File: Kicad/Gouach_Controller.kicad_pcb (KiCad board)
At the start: 4 copper layers, 41 x 104 mm, 135 parts, among them J1 HALL/Encoder, J10 USB, J11 CANBUS, J12 Serial, J2 SWD, J3 Peripherals, J4 IN+, J5 IN-, J6 MOTOR3, J7 MOTOR2, J8 MOTOR1, Q1 IRFB7530, Q2 IRFB7530, Q3 IRFB7530, Q4 IRFB7530, Q5 IRFB7530, Q6 IRFB7530, U1 STM32F405RGT6, U2 TC2117, U3 DRV8302, U4 SN65HVD232, U5 TPS54360DDA, Y2 8MHz

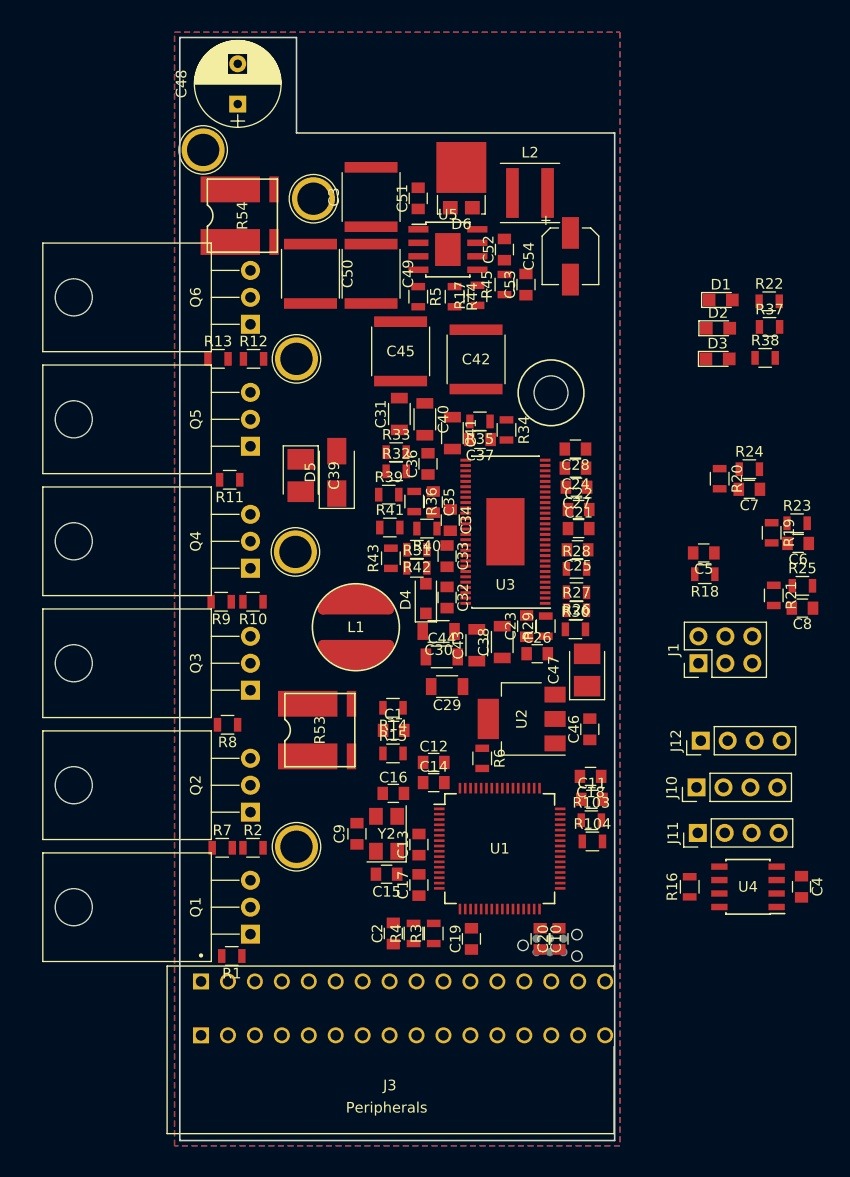
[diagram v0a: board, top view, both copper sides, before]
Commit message: Passives changed from 0805 to 0603
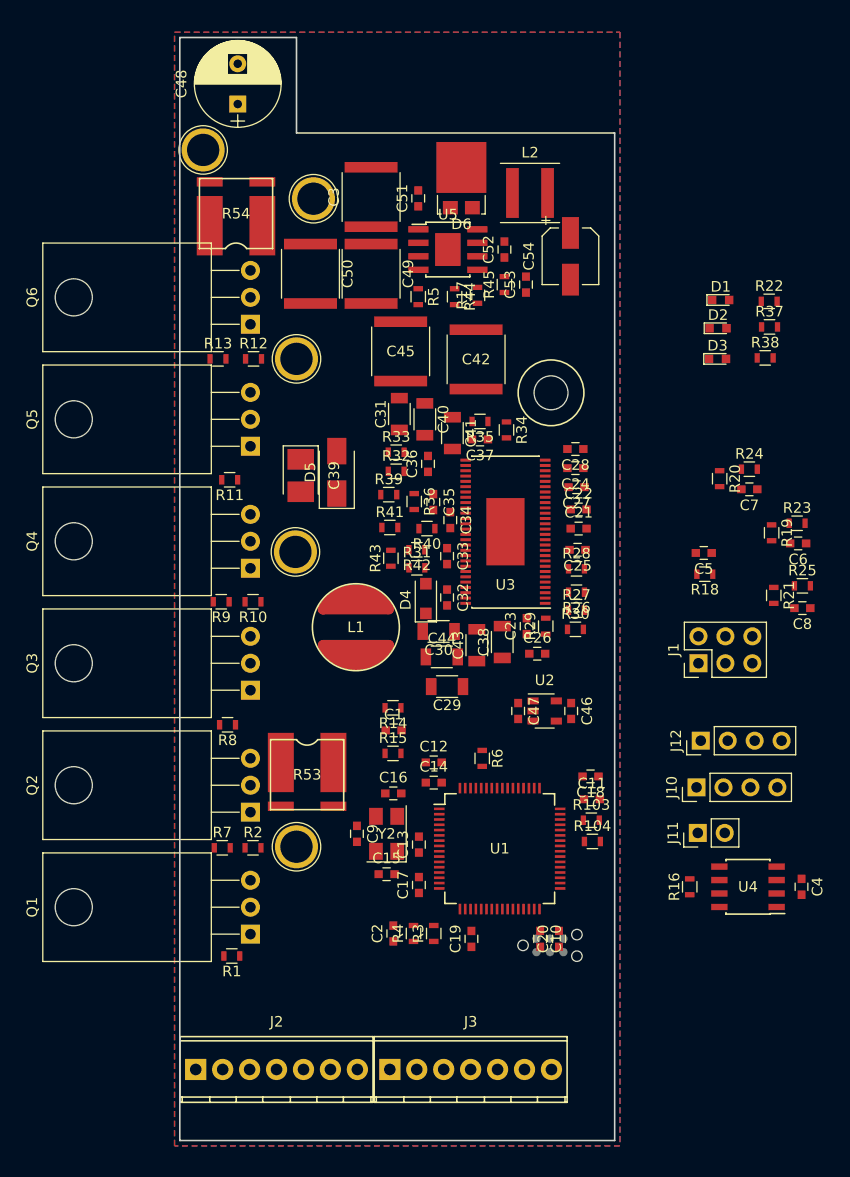
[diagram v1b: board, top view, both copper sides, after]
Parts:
- added J2: Peripherals, Romain:TerminalBlock_Phoenix_MPT-2.54mm_7pol, F.Cu at (101.5, 143.3)
- C1, C10, C11, C12, C13, C14, C15, C16, C17, C18, C19, C2, C20, C21, C22, C23, C24, C25, C26, C27, C28, C32, C33, C34, C35, C36, C37, C4, C5, C51, C52, C53, C6, C7, C8, C9: footprint Capacitors_SMD:C_0805 -> Capacitors_SMD:C_0603
- C46: value 2.2uF -> 10uF; footprint Capacitors_SMD:C_0805 -> Capacitors_SMD:C_0603
- C47: value 15uF/100V -> 10uF; footprint Capacitors_Tantalum_SMD:CP_Tantalum_Case-B_EIA-3528-21_Reflow -> Capacitors_SMD:C_0603
- D1, D2, D3: footprint LEDs:LED_0805 -> LEDs:LED_0603
- J11: footprint Pin_Headers:Pin_Header_Straight_1x04_Pitch2.54mm -> Pin_Headers:Pin_Header_Straight_1x02_Pitch2.54mm
- J3: footprint Romain:TBL009-254-16BE-2BE -> Romain:TerminalBlock_Phoenix_MPT-2.54mm_7pol
- Q1, Q2, Q3, Q4, Q5, Q6: footprint TO_SOT_Packages_THT:TO-220-3_Horizontal -> Romain:TO-220-3_Horizontal
- R1, R10, R103, R104, R11, R12, R13, R14, R15, R16, R17, R18, R19, R2, R20, R21, R22, R23, R24, R25, R26, R27, R28, R29, R3, R30, R31, R32, R33, R34, R35, R36, R37, R38, R39, R4, R40, R41, R42, R43, R44, R45, R5, R6, R7, R8, R9: footprint Resistors_SMD:R_0805 -> Resistors_SMD:R_0603
- U2: value TC2117 -> XC6220B331MR; footprint TO_SOT_Packages_SMD:SOT-223-3_TabPin2 -> TO_SOT_Packages_SMD:SOT-23-5
- moved J3 19.6 mm to (119.8, 143.3)
- moved C47 7.56 mm to (131.9, 109.5), turned to 270 degrees
- moved R53 4.37 mm to (112.0, 115.5), turned to 180 degrees
- moved C46 2.46 mm to (136.9, 109.5), turned to 270 degrees
- moved U2 2.29 mm to (134.4, 109.5), turned to 0 degrees
- moved R54 0.63 mm to (105.3, 62.6), turned to 0 degrees
- renumbered J2 to J9
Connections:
- C47 pad 1: +3V3 -> +5V
- J11 pad 1: +5V -> /CAN Transceiver/CAN_P
- J11 pad 2: /CAN Transceiver/CAN_P -> /CAN Transceiver/CAN_N
- J3 pad 1: +5V -> GND
- J3 pad 2: /ADC_THROTTLE -> +5V
- J3 pad 3: GND -> /IO_BRAKE
- J3 pad 4: +5V -> /ADC_BRAKE
- J3 pad 5: /PFS -> GND
- J3 pad 6: /ADC_TORQUE -> Net-(J3-Pad6)
- J3 pad 7: /CRUISE -> GND
- U1 pad 20: /MCU/TX_SDA_NSS -> /TX
- U1 pad 23: /MCU/RX_SCL_MOSI -> /RX
- U1 pad 29: /MCU/RX_SCL_MOSI -> /RX
- U1 pad 30: /MCU/TX_SDA_NSS -> /TX
- U1 pad 37: /MCU/TX_SDA_NSS -> /TX
- U1 pad 38: /MCU/RX_SCL_MOSI -> /RX
- U2 pad 1: GND -> +5V
- U2 pad 2: +3V3 -> GND

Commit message: Components placed
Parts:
- removed R103, R104: 22R, Resistors_SMD:R_0603
- added Q7: DMN3300U, TO_SOT_Packages_SMD:SOT-23, F.Cu at (132.8, 66.8)
- added R46: 100R, Resistors_SMD:R_0603, F.Cu at (129.7, 67.8)
- added R47: 10k, Resistors_SMD:R_0603, F.Cu at (129.7, 65.9)
- added U6: USBLC6-2SC6, TO_SOT_Packages_SMD:SOT-23-6, F.Cu at (135.4, 70.7)
- C12, C14, C16, C17, C18, C19, C20: value 2.2uF -> 100nF
- C3, C49, C50: footprint Capacitors_SMD:C_2220 -> Capacitors_SMD:C_1210
- D4: value 60V 2A -> 60V
- D6: value 100V -> 60V; footprint TO_SOT_Packages_SMD:TO-277A -> Diodes_SMD:D_SOD-123F
- J9: moved to F.Cu
- moved D1 78.9 mm to (138.9, 148.7), turned to 180 degrees
- moved R37 75.9 mm to (138.9, 147.3), turned to 180 degrees
- moved D2 73.4 mm to (138.9, 145.9), turned to 180 degrees
- moved R22 72.7 mm to (138.9, 141.7), turned to 180 degrees
- moved R38 70.2 mm to (138.9, 144.5), turned to 180 degrees
- moved D3 67.8 mm to (138.9, 143.1), turned to 180 degrees
- moved R24 54.6 mm to (118.5, 128.4), turned to 90 degrees
- moved R20 54.3 mm to (117.8, 130.6), turned to 180 degrees
- moved C7 54.1 mm to (117.0, 128.4), turned to 270 degrees
- moved R18 53.5 mm to (116.8, 139.0)
- moved J12 53.4 mm to (101.8, 136.9)
- moved C5 53.3 mm to (119.8, 139.0), turned to 0 degrees
- moved C8 53.1 mm to (114.0, 128.4), turned to 270 degrees
- moved R25 53.0 mm to (115.5, 128.4), turned to 90 degrees
- moved R21 52.2 mm to (114.7, 130.6), turned to 180 degrees
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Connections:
- D4 pad 1: GND -> Net-(C32-Pad1)
- D4 pad 2: Net-(C32-Pad1) -> GND
- D5 pad 1: GND -> +5V
- D5 pad 2: +5V -> GND
- J10 pad 2: /D+ -> /D-
- J10 pad 3: /D- -> /D+
- Q3 pad 3: /MOSFETs driver/H2_VS -> /MOSFETs driver/H3_VS
- Q4 pad 2: /MOSFETs driver/H2_VS -> /MOSFETs driver/H3_VS
- Q4 pad 3: GND -> /MOSFETs driver/H3_LOW
- Q5 pad 3: /MOSFETs driver/H3_VS -> /MOSFETs driver/H2_VS
- Q6 pad 2: /MOSFETs driver/H3_VS -> /MOSFETs driver/H2_VS
- Q6 pad 3: /MOSFETs driver/H3_LOW -> GND
- R10 pad 2: Net-(Q4-Pad1) -> Net-(Q6-Pad1)
- R11 pad 1: Net-(Q5-Pad1) -> Net-(Q3-Pad1)
- R12 pad 1: Net-(Q6-Pad1) -> Net-(Q4-Pad1)
- R13 pad 2: Net-(Q6-Pad1) -> Net-(Q4-Pad1)
- R8 pad 1: Net-(Q3-Pad1) -> Net-(Q5-Pad1)
- R9 pad 1: Net-(Q4-Pad1) -> Net-(Q6-Pad1)
- U1 pad 11: Net-(U1-Pad11) -> /MCU/LAMP_CMD
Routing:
- net +5V: track 0.00 -> 48.6 mm
- net +3V3: track 0.00 -> 21.4 mm, vias 0 -> 3
- net +BATT: track 0.00 -> 15.5 mm, vias 0 -> 119
- net +5VP: track 0.00 -> 12.2 mm
- net Net-(C24-Pad2): track 0.00 -> 11.5 mm, vias 0 -> 2
- net GND: track 0.00 -> 9.10 mm
- net /MCU/OSC_IN: track 0.00 -> 8.96 mm
- net Net-(C51-Pad2): track 0.00 -> 8.15 mm, vias 0 -> 2
- net /MCU/OSC_OUT: track 0.00 -> 5.89 mm
- net /CAN Transceiver/CAN_P: track 0.00 -> 5.40 mm
- net /CAN Transceiver/CAN_N: track 0.00 -> 5.40 mm
- net Net-(C21-Pad1): track 0.00 -> 5.37 mm
- net /Filters/HALL1_IN: track 0.00 -> 5.06 mm
- net /Filters/HALL3_IN: track 0.00 -> 5.05 mm
- net /Filters/HALL2_IN: track 0.00 -> 4.85 mm
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- added copper zone on F.Cu, net +5VP
- added copper zone on B.Cu, net +BATT
- added copper zone on F.Cu, net +BATT
- added copper zone on GND, net +BATT
- added copper zone on GND2, net +BATT
- added copper zone on F.Cu, net Net-(C51-Pad2)
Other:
- outline, holes or cut-outs redrawn
- net class Default: clearance 0.1778 -> 0.2; trace_width 0.2032 -> 0.254; via_dia 0.8 -> 0.5; via_drill 0.5 -> 0.3
- rule trace_clearance: 0.1778 -> 0.2
- rule via_min_drill: 0.5 -> 0.3
- rule via_min_size: 0.8 -> 0.5
- board text added: "5V Thr GND 5V PFS Trq Crs GND 5V BkD BkA GND Lmp GND"

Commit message: Routing done
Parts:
- removed C42, C45: 15uF/100V, Capacitors_SMD:C_2220
- added C55: 2.2uF, Capacitors_SMD:C_1210, F.Cu at (122.2, 114.6)
- added C56: 100nF, Capacitors_SMD:C_0603, F.Cu at (121.5, 127.4)
- added G***: LOGO, Romain:logo, B.Cu at (120.4, 137.3)
- C22, C24: value 2.2uF -> NP
- C25, C28: value 2.2uF -> 1uF
- C29: value 10uF/60V -> 2.2uF; footprint Capacitors_SMD:C_1206 -> Capacitors_SMD:C_1210
- C30, C38: value 10uF/60V -> 100nF; footprint Capacitors_SMD:C_1206 -> Capacitors_SMD:C_0805
- C31: value 10uF/60V -> 47uF; footprint Capacitors_SMD:C_1206 -> Capacitors_SMD:C_1210
- C33, C34, C35: value 220nF -> 100nF
- C36, C37: value 2.2nF -> 1nF
- C39: value 15uF/100V -> 1uF; footprint Capacitors_Tantalum_SMD:CP_Tantalum_Case-B_EIA-3528-21_Reflow -> Capacitors_SMD:C_0603
- C40, C41, C43, C44: value 10uF/60V -> 10uF
- C48: footprint Capacitors_THT:CP_Radial_D8.0mm_P3.80mm -> Romain:Capacitor_Horizontal
- J11: value CANBUS -> CAN
- J12: moved to B.Cu
- J4, J5: footprint Connectors:1pin -> Mounting_Holes:MountingHole_2.7mm_Pad_Via
- J6, J7, J8: footprint Connectors:1pin -> Mounting_Holes:MountingHole_2.2mm_M2_Pad_Via
- moved C3 78.4 mm to (101.9, 136.7), turned to 270 degrees
- moved C50 77.6 mm to (105.2, 136.7), turned to 270 degrees
- moved C49 77.3 mm to (108.5, 136.7), turned to 270 degrees
- moved C54 75.4 mm to (132.4, 135.5)
- moved R45 75.3 mm to (119.9, 138.6)
- moved R44 75.2 mm to (123.1, 138.6), turned to 0 degrees
- moved L2 75.2 mm to (126.4, 134.5)
- moved J12 74.8 mm to (139.4, 72.3), turned to 0 degrees
- moved C52 74.8 mm to (119.2, 135.9)
- moved C53 74.8 mm to (120.7, 135.9)
- moved R5 74.8 mm to (112.4, 139.3)
- moved U5 74.8 mm to (114.5, 135.9)
- moved D6 74.4 mm to (116.4, 131.8)
- moved J11 73.8 mm to (136.6, 61.7), turned to 90 degrees
- moved C51 73.6 mm to (112.4, 132.2), turned to 0 degrees
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- renumbered Q6 to Q4, Q4 to Q6
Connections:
- net +5VP renamed VBUS
- C31 pad 1: +BATT -> +5V
- C40 pad 1: GND -> +BATT
- C40 pad 2: +BATT -> GND
- C41 pad 1: GND -> +BATT
- C41 pad 2: +BATT -> GND
- C43 pad 1: GND -> +BATT
- C43 pad 2: +BATT -> GND
- C44 pad 1: GND -> +BATT
- C44 pad 2: +BATT -> GND
- J1 pad 3: /Filters/TEMP_IN -> GND
- J1 pad 5: GND -> /Filters/TEMP_IN
- Q3 pad 3: /MOSFETs driver/H3_VS -> /MOSFETs driver/H2_VS
- Q5 pad 3: /MOSFETs driver/H2_VS -> /MOSFETs driver/H3_VS
- R11 pad 1: Net-(Q3-Pad1) -> Net-(Q5-Pad1)
- R32 pad 1: /MOSFETs driver/SH1_A -> /MOSFETs driver/SH1+
- R33 pad 1: /MOSFETs driver/SH1_B -> /MOSFETs driver/SH1-
- R34 pad 1: /MOSFETs driver/SH2_A -> /MOSFETs driver/SH2+
- R35 pad 1: /MOSFETs driver/SH2_B -> /MOSFETs driver/SH2-
- R53 pad 1: GND -> /MOSFETs driver/H1_LOW
- R53 pad 2: /MOSFETs driver/SH2_B -> /MOSFETs driver/SH2+
- R53 pad 3: /MOSFETs driver/SH2_A -> /MOSFETs driver/SH2-
- R53 pad 4: /MOSFETs driver/H1_LOW -> GND
- R54 pad 1: GND -> /MOSFETs driver/H3_LOW
- R54 pad 2: /MOSFETs driver/SH1_B -> /MOSFETs driver/SH1+
- R54 pad 3: /MOSFETs driver/SH1_A -> /MOSFETs driver/SH1-
- R54 pad 4: /MOSFETs driver/H3_LOW -> GND
- R8 pad 1: Net-(Q5-Pad1) -> Net-(Q3-Pad1)
- U1 pad 20: /TX -> Net-(U1-Pad20)
- U1 pad 23: /RX -> Net-(U1-Pad23)
- U1 pad 37: /TX -> Net-(U1-Pad37)
- U1 pad 38: /RX -> Net-(U1-Pad38)
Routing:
- net +3V3: track 21.4 -> 207.2 mm, vias 3 -> 10
- net /CRUISE: track 0.00 -> 107.6 mm, vias 0 -> 2
- net /MCU/LED_RED: track 0.00 -> 99.7 mm, vias 0 -> 2
- net /ADC_THROTTLE: track 0.00 -> 99.6 mm, vias 0 -> 2
- net /IO_BRAKE: track 0.00 -> 99.3 mm, vias 0 -> 1
- net /MCU/AN_IN: track 0.00 -> 96.0 mm, vias 0 -> 4
- net /PFS: track 0.00 -> 95.5 mm, vias 0 -> 1
- net /MCU/LED_GREEN: track 0.00 -> 95.5 mm, vias 0 -> 2
- net /ADC_TORQUE: track 0.00 -> 90.9 mm, vias 0 -> 1
- net +5V: track 48.6 -> 138.0 mm, vias 0 -> 4
- net /ADC_BRAKE: track 0.00 -> 87.1 mm, vias 0 -> 1
- net /MCU/LAMP_CMD: track 0.00 -> 84.1 mm, vias 0 -> 2
- net /MCU/USB_D+: track 0.00 -> 77.6 mm, vias 0 -> 2
- net /MCU/USB_D-: track 0.00 -> 76.8 mm, vias 0 -> 2
- net +BATT: track 15.5 -> 84.4 mm, vias 119 -> 131
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- added copper zone on F.Cu, net +5V
- added copper zone on In1.Cu, net +BATT
- added copper zone on In2.Cu, net +BATT
- added copper zone on B.Cu, net /MOSFETs driver/H1_LOW
- added copper zone on F.Cu, net /MOSFETs driver/H1_LOW
- added copper zone on In1.Cu, net /MOSFETs driver/H1_LOW
- added copper zone on In2.Cu, net /MOSFETs driver/H1_LOW
- added copper zone on B.Cu, net /MOSFETs driver/H1_VS
- added copper zone on F.Cu, net /MOSFETs driver/H1_VS
- added copper zone on In1.Cu, net /MOSFETs driver/H1_VS
- added copper zone on In2.Cu, net /MOSFETs driver/H1_VS
- added copper zone on B.Cu, net /MOSFETs driver/H2_VS
- added copper zone on F.Cu, net /MOSFETs driver/H2_VS
- added copper zone on In1.Cu, net /MOSFETs driver/H2_VS
- added copper zone on In2.Cu, net /MOSFETs driver/H2_VS
- added copper zone on B.Cu, net /MOSFETs driver/H3_LOW
- added copper zone on F.Cu, net /MOSFETs driver/H3_LOW
- added copper zone on In1.Cu, net /MOSFETs driver/H3_LOW
- added copper zone on In2.Cu, net /MOSFETs driver/H3_LOW
- added copper zone on B.Cu, net /MOSFETs driver/H3_VS
- added copper zone on F.Cu, net /MOSFETs driver/H3_VS
- added copper zone on In1.Cu, net /MOSFETs driver/H3_VS
- added copper zone on In2.Cu, net /MOSFETs driver/H3_VS
- added copper zone on In1.Cu, net GND
- added copper zone on In2.Cu, net GND
- removed copper zone on GND, net +BATT
- removed copper zone on GND2, net +BATT
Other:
- outline, holes or cut-outs redrawn
- board text added: "+ -"
- board text added: "3/T 2/G 1/5"
- board text added: "5V D- D+ GND"
- board text added: "5V Thr GND 5V PFS Trq Crs"
- board text added: "GND 5V BkD BkA GND Lmp GND"
- board text added: "GND RX TX 5V"
- board text added: "TEMP HALL3 GND HALL2 +5V HALL1"
- board text removed: "5V Thr GND 5V PFS Trq Crs GND 5V BkD BkA GND Lmp GND"

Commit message: Fixed libraries issues
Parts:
- C1, C10, C11, C12, C13, C14, C15, C16, C17, C18, C19, C2, C20, C21, C22, C23, C24, C25, C26, C27, C28, C32, C33, C34, C35, C36, C37, C39, C4, C46, C47, C5, C51, C52, C53, C56, C6, C7, C8, C9: footprint Capacitors_SMD:C_0603 -> Capacitor_SMD:C_0603_1608Metric
- C29, C31, C55: footprint Capacitors_SMD:C_1210 -> Capacitor_SMD:C_1210_3225Metric
- C3, C49, C50: footprint Capacitors_SMD:C_1210 -> Capacitor_SMD:C_1206_3216Metric
- C30, C38: footprint Capacitors_SMD:C_0805 -> Capacitor_SMD:C_0805_2012Metric
- C40, C41, C43, C44: footprint Capacitors_SMD:C_1206 -> Capacitor_SMD:C_1206_3216Metric
- C48: value 15uF/100V -> 15uF; footprint Romain:Capacitor_Horizontal -> Gouach-Controller:Capacitor_Horizontal
- C54: footprint Capacitors_SMD:CP_Elec_5x5.8 -> Capacitor_SMD:C_Elec_5x5.8
- D1, D2, D3: footprint LEDs:LED_0603 -> LED_SMD:LED_0603_1608Metric
- D4, D6: footprint Diodes_SMD:D_SOD-123F -> Diode_SMD:D_SOD-123F
- D5: footprint Diodes_SMD:D_SMA -> Diode_SMD:D_SMA
- H1: footprint Mounting_Holes:MountingHole_3.2mm_M3 -> MountingHole:MountingHole_3.2mm_M3
- J1: footprint Pin_Headers:Pin_Header_Straight_2x03_Pitch2.54mm -> Connector_PinHeader_2.54mm:PinHeader_2x03_P2.54mm_Vertical
- J10, J12: footprint Pin_Headers:Pin_Header_Straight_1x04_Pitch2.54mm -> Connector_PinHeader_2.54mm:PinHeader_1x04_P2.54mm_Vertical
- J11: footprint Pin_Headers:Pin_Header_Straight_1x02_Pitch2.54mm -> Connector_PinHeader_2.54mm:PinHeader_1x02_P2.54mm_Vertical
- J2, J3: footprint Romain:TerminalBlock_Phoenix_MPT-2.54mm_7pol -> Gouach-Controller:TerminalBlock_Phoenix_MPT-2.54mm_7pol
- J4: value IN+ -> BAT+; footprint Mounting_Holes:MountingHole_2.7mm_Pad_Via -> MountingHole:MountingHole_2.7mm_Pad_Via
- J5: value IN- -> BAT-; footprint Mounting_Holes:MountingHole_2.7mm_Pad_Via -> MountingHole:MountingHole_2.7mm_Pad_Via
- J6: value MOTOR3 -> M1; footprint Mounting_Holes:MountingHole_2.2mm_M2_Pad_Via -> MountingHole:MountingHole_2.2mm_M2_Pad_Via
- J7: value MOTOR2 -> M2; footprint Mounting_Holes:MountingHole_2.2mm_M2_Pad_Via -> MountingHole:MountingHole_2.2mm_M2_Pad_Via
- J8: value MOTOR1 -> M3; footprint Mounting_Holes:MountingHole_2.2mm_M2_Pad_Via -> MountingHole:MountingHole_2.2mm_M2_Pad_Via
- J9: footprint Connectors:Tag-Connect_TC2030-IDC-NL -> Connector:Tag-Connect_TC2030-IDC-NL_2x03_P1.27mm_Vertical
- L1: footprint Romain:SDR0805 -> Gouach-Controller:SDR0805
- L2: footprint Inductors_SMD:L_Coilcraft_XAL5030 -> Inductor_SMD:L_Coilcraft_XAL5030
- Q1, Q2, Q3, Q4, Q5, Q6: footprint Romain:TO-220-3_Horizontal -> Gouach-Controller:TO-220-3_Horizontal
- Q7: footprint TO_SOT_Packages_SMD:SOT-23 -> Package_TO_SOT_SMD:SOT-23
- R1, R10, R11, R12, R13, R14, R15, R16, R17, R18, R19, R2, R20, R21, R22, R23, R24, R25, R26, R27, R28, R29, R3, R30, R31, R32, R33, R34, R35, R36, R37, R38, R39, R4, R40, R41, R42, R43, R44, R45, R46, R47, R5, R6, R7, R8, R9: footprint Resistors_SMD:R_0603 -> Resistor_SMD:R_0603_1608Metric
- R53, R54: footprint Romain:WSLP2726 -> Gouach-Controller:WSLP2726
- U1: footprint Housings_QFP:LQFP-64_10x10mm_Pitch0.5mm -> Package_QFP:LQFP-64_10x10mm_P0.5mm
- U2: footprint TO_SOT_Packages_SMD:SOT-23-5 -> Package_TO_SOT_SMD:SOT-23-5
- U3: footprint Romain:DRV8302 -> Gouach-Controller:DRV8302
- U4: footprint Housings_SOIC:SOIC-8_3.9x4.9mm_Pitch1.27mm -> Package_SO:SOIC-8_3.9x4.9mm_P1.27mm
- U5: footprint Housings_SOIC:TI_SO-PowerPAD-8 -> Package_SO:TI_SO-PowerPAD-8
- U6: footprint TO_SOT_Packages_SMD:SOT-23-6 -> Package_TO_SOT_SMD:SOT-23-6
- Y2: footprint Crystals:Crystal_SMD_5032-4pin_5.0x3.2mm -> Crystal:Crystal_SMD_5032-4Pin_5.0x3.2mm
- moved C10 1.21 mm to (133.9, 61.1)
- moved C17 0.89 mm to (129.0, 76.6)
- moved J9 0.40 mm to (117.4, 60.7)
- moved C15 0.38 mm to (127.4, 77.1)
- moved D1 0.38 mm to (120.4, 145.8)
- moved D2 0.38 mm to (120.4, 148.9)
- moved D3 0.38 mm to (120.4, 142.8)
- moved R22 0.38 mm to (120.4, 141.2)
- moved R37 0.38 mm to (120.4, 144.3)
- moved R38 0.38 mm to (120.4, 147.3)
- moved R6 0.36 mm to (119.2, 67.6)
- moved C13 0.28 mm to (126.9, 74.3)
- moved C19 0.25 mm to (134.2, 71.4)
- moved C16 0.25 mm to (122.2, 74.3)
- moved C9 0.25 mm to (120.3, 77.1)
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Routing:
- net /Filters/TEMP_IN: track 21.9 -> 25.8 mm, vias 2 -> 1
- net +3V3: track 207.2 -> 205.3 mm, vias 10 -> 11
- net /MCU/USB_D+: track 77.6 -> 76.0 mm
- net Net-(C26-Pad2): track 1.41 -> 2.92 mm
- net BOOT0: track 13.0 -> 14.5 mm
- net Net-(C10-Pad1): track 1.75 -> 2.82 mm
- net NRST: track 18.8 -> 19.9 mm
- net +5V: track 138.0 -> 138.9 mm
- net /CAN Transceiver/CAN_RX: track 22.0 -> 21.1 mm
- net /Filters/HALL2_OUT: track 24.3 -> 25.2 mm
- net SWCLK: track 7.29 -> 8.12 mm
- net /Filters/HALL1_OUT: track 31.7 -> 32.5 mm
- net Net-(C24-Pad2): track 13.7 -> 14.3 mm
- net /MOSFETs driver/SH2+: track 27.9 -> 27.3 mm
- net /MCU/AN_IN: track 96.0 -> 95.5 mm
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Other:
- rule trace_min: 0.2032 -> 0
